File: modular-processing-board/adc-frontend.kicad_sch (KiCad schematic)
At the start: 70 parts, among them J1001 BWU.FL-IPEX1, J601 Conn_Coaxial_Small, J602 BWU.FL-IPEX1, J604 Conn_Coaxial_Small, U1002 THS4521IDGK, U601 LMV321, U602 TL432DBZ, U603 THS4521IDGK

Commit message: matched PSSI bus lenghts
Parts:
- C1012, C1016, C609, C615: LCSC Part Number C1634 -> (none); Manufacturing Part Number CL10C100JB8NNNC -> (none)
- C1015, C611: LCSC Part Number C1664 -> (none); Manufacturing Part Number CL10C331JB8NNNC -> (none)
- C1024, C601, C604, C605, C606, C607, C608, C617: LCSC Part Number C22435929 -> (none); Manufacturing Part Number CGA0201X7R104K160ET -> (none)
- C1025, C602, C618: LCSC Part Number C285010 -> (none); Manufacturing Part Number 0201B103K250NT -> (none)
- C603: LCSC Part Number C16772 -> (none); Manufacturing Part Number CL05B224KO5NNNC -> (none)
- C610, C612, C613, C614: LCSC Part Number C88136 -> (none); Manufacturing Part Number 0603B104J500NT -> (none)
- C616, C619: LCSC Part Number C23733 -> (none); Manufacturing Part Number CL05A475MP5NRNC -> (none)
- J1001, J602: LCSC Part Number C5137195 -> (none); Manufacturing Part Number BWU.FL-IPEX1 -> (none)
- J601, J604: LCSC Part Number C496549 -> (none); Manufacturing Part Number BWSMA-KE-Z001 -> (none)
- R1001, R620: LCSC Part Number C21189 -> (none); Manufacturing Part Number 0603WAF0000T5E -> (none)
- R1006, R608, R609, R610, R612, R627, R628, R629: LCSC Part Number C25804 -> (none); Manufacturing Part Number 0603WAF1002T5E -> (none)
- R1009, R1013, R1021, R1024, R601, R611, R613, R619, R621: LCSC Part Number C21190 -> (none); Manufacturing Part Number 0603WAF1001T5E -> (none)
- R1015, R616: LCSC Part Number C17168 -> (none); Manufacturing Part Number 0402WGF0000TCE -> (none)
- R1016, R1019, R614, R615, R617, R618, R625, R626: LCSC Part Number C23182 -> (none); Manufacturing Part Number 0603WAF470JT5E -> (none)
- R602: LCSC Part Number C4275 -> (none); Manufacturing Part Number 0603WAF750JT5E -> (none)
- R603, R605, R606: LCSC Part Number 0603WAF1001T5E -> (none); Manufacturing Part Number C21190 -> (none)
- R604: LCSC Part Number C22843 -> (none); Manufacturing Part Number 0603WAF1501T5E -> (none)
- R607: LCSC Part Number C23162 -> (none); Manufacturing Part Number 0603WAF4701T5E -> (none)
- U1002, U603: LCSC Part Number C170157 -> (none); Manufacturing Part Number THS4521IDGKR -> (none)
- U601: LCSC Part Number C7972 -> (none); Manufacturing Part Number LMV321IDBVR -> (none)
- U602: LCSC Part Number C5184435 -> (none); Manufacturing Part Number TL432 -> (none)

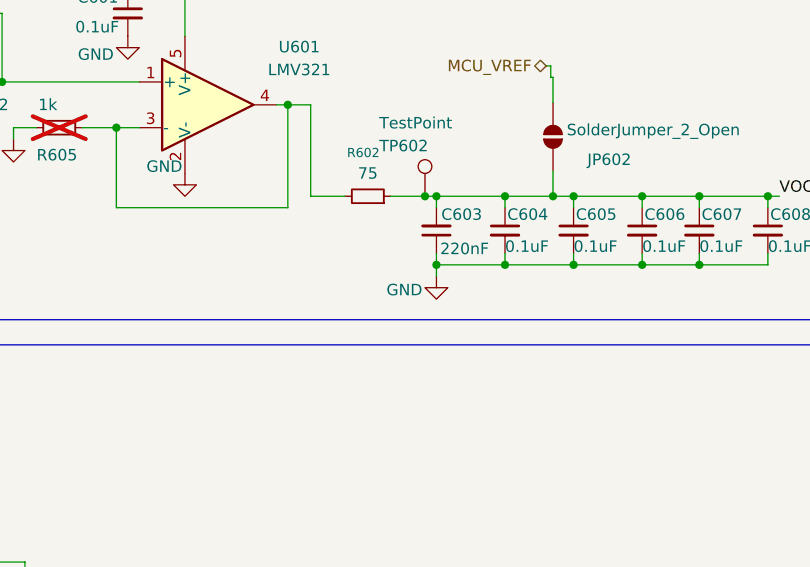
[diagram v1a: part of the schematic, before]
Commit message: finish modular-processing-hw board checks, prepare gerbers for manufacturing and perform checks
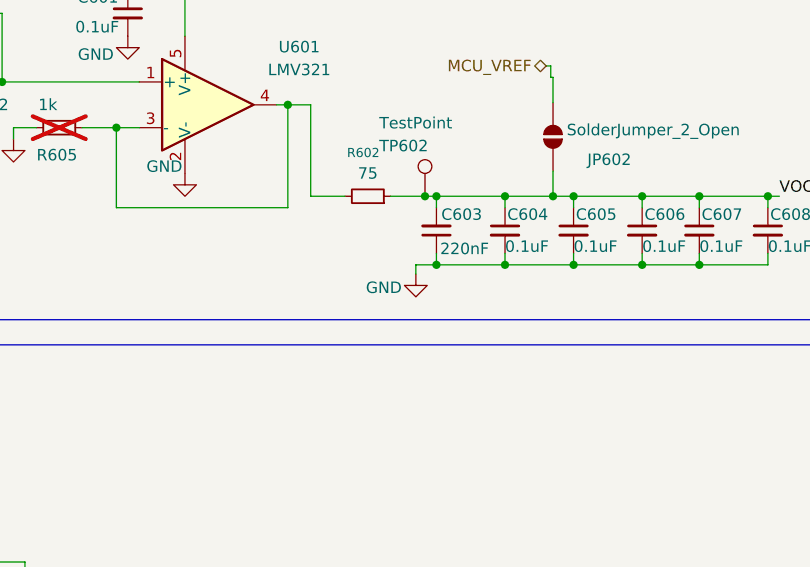
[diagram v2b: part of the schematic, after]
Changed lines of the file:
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@@
 	(wire
 		(pts
-			(xy 181.61 68.58) (xy 181.61 67.31)
+			(xy 179.324 68.326) (xy 179.324 67.31)
 		)
 		(stroke
@@
 	(wire
 		(pts
+			(xy 179.324 67.31) (xy 181.61 67.31)
+		)
+		(stroke
+			(width 0)
+			(type default)
+		)
+	)
+	(wire
+		(pts
 			(xy 175.26 123.19) (xy 175.26 127)
 		)
@@
 	(symbol
 		(lib_id "power:GND")
-		(at 181.61 68.58 0)
+		(at 179.324 68.326 0)
 		(mirror y)
 		(unit 1)
@@
 		(dnp no)
 		(property "Reference" "#PWR0607"
-			(at 181.61 74.93 0)
+			(at 179.324 74.676 0)
 			(effects
 				(font
@@
 		)
 		(property "Value" "GND"
-			(at 178.054 70.104 0)
+			(at 175.768 69.85 0)
 			(effects
 				(font
@@
 		)
 		(property "Footprint" ""
-			(at 181.61 68.58 0)
+			(at 179.324 68.326 0)
 			(effects
 				(font
@@
 		)
 		(property "Datasheet" ""
-			(at 181.61 68.58 0)
+			(at 179.324 68.326 0)
 			(effects
 				(font
@@
 		)
 		(property "Description" "Power symbol creates a global label with name \"GND\" , ground"
-			(at 181.61 68.58 0)
+			(at 179.324 68.326 0)
 			(effects
 				(font

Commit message: minor changes in BOM and DNP-components
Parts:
- C1025, C602, C618: footprint Capacitor_SMD:C_0201_0603Metric -> Capacitor_SMD:C_0402_1005Metric; LPN C285010 -> C15195; MPN 0201B103K250NT -> CL05B103KB5NNNC
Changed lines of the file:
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@@
 			)
 		)
-		(property "Footprint" "Capacitor_SMD:C_0201_0603Metric"
+		(property "Footprint" "Capacitor_SMD:C_0402_1005Metric"
 			(at 113.03 146.05 0)
 			(effects
@@
 			)
 		)
-		(property "LPN" "C285010 "
+		(property "LPN" "C15195"
 			(at 113.03 146.05 0)
 			(effects
@@
 			)
 		)
-		(property "MPN" "0201B103K250NT"
+		(property "MPN" "CL05B103KB5NNNC"
 			(at 113.03 146.05 0)
 			(effects
@@
 			)
 		)
-		(property "Footprint" "Capacitor_SMD:C_0201_0603Metric"
+		(property "Footprint" "Capacitor_SMD:C_0402_1005Metric"
 			(at 121.92 255.27 0)
 			(effects
@@
 			)
 		)
-		(property "LPN" "C285010 "
+		(property "LPN" "C15195"
 			(at 121.92 255.27 0)
 			(effects
@@
 			)
 		)
-		(property "MPN" "0201B103K250NT"
+		(property "MPN" "CL05B103KB5NNNC"
 			(at 121.92 255.27 0)
 			(effects
@@
 			)
 		)
-		(property "Footprint" "Capacitor_SMD:C_0201_0603Metric"
+		(property "Footprint" "Capacitor_SMD:C_0402_1005Metric"
 			(at 127 50.8 0)
 			(effects
@@
 			)
 		)
-		(property "LPN" "C285010 "
+		(property "LPN" "C15195"
 			(at 127 50.8 0)
 			(effects
@@
 			)
 		)
-		(property "MPN" "0201B103K250NT"
+		(property "MPN" "CL05B103KB5NNNC"
 			(at 127 50.8 0)
 			(effects

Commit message: changed footprints (next) try uploading to jlcpcb for manufacturing, change crystal if required for economic assembly
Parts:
- C610, C612, C613, C614: value 100 nF +-5% -> 100nF; footprint Capacitor_SMD:C_0603_1608Metric_Pad1.08x0.95mm_HandSolder -> Capacitor_SMD:C_0603_1608Metric; LPN C88136 -> C14663; MPN 0603B104J500NT -> CC0603KRX7R9BB104
- R1001, R620: footprint Resistor_SMD:R_0603_1608Metric_Pad0.98x0.95mm_HandSolder -> Resistor_SMD:R_0603_1608Metric
- R1015, R616: footprint Resistor_SMD:R_0402_1005Metric_Pad0.72x0.64mm_HandSolder -> Resistor_SMD:R_0603_1608Metric; LPN C17168 -> C21189; MPN 0402WGF0000TCE -> 0603WAF0000T5E
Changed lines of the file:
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@@
 			)
 		)
-		(property "Value" "100 nF +-5%"
+		(property "Value" "100nF"
 			(at 54.102 128.524 90)
 			(effects
@@
 			)
 		)
-		(property "Footprint" "Capacitor_SMD:C_0603_1608Metric_Pad1.08x0.95mm_HandSolder"
+		(property "Footprint" "Capacitor_SMD:C_0603_1608Metric"
 			(at 46.99 125.73 0)
 			(effects
@@
 			)
 		)
-		(property "LPN" "C88136"
+		(property "LPN" "C14663"
 			(at 46.99 125.73 90)
 			(effects
@@
 			)
 		)
-		(property "MPN" "0603B104J500NT"
+		(property "MPN" "CC0603KRX7R9BB104"
 			(at 46.99 125.73 90)
 			(effects
@@
 			)
 		)
-		(property "Footprint" "Resistor_SMD:R_0603_1608Metric_Pad0.98x0.95mm_HandSolder"
+		(property "Footprint" "Resistor_SMD:R_0603_1608Metric"
 			(at 175.26 140.97 0)
 			(effects
@@
 			)
 		)
-		(property "Footprint" "Resistor_SMD:R_0402_1005Metric_Pad0.72x0.64mm_HandSolder"
+		(property "Footprint" "Resistor_SMD:R_0603_1608Metric"
 			(at 95.25 242.57 0)
 			(effects
@@
 			)
 		)
-		(property "LPN" "C17168"
+		(property "LPN" "C21189"
 			(at 95.25 242.57 90)
 			(effects
@@
 			)
 		)
-		(property "MPN" "0402WGF0000TCE"
+		(property "MPN" "0603WAF0000T5E"
 			(at 95.25 242.57 90)
 			(effects
@@
 			)
 		)
-		(property "Footprint" "Resistor_SMD:R_0603_1608Metric_Pad0.98x0.95mm_HandSolder"
+		(property "Footprint" "Resistor_SMD:R_0603_1608Metric"
 			(at 175.26 120.65 0)
 			(effects
@@
 			)
 		)
-		(property "Value" "100 nF +-5%"
+		(property "Value" "100nF"
 			(at 55.372 138.43 90)
 			(effects
@@
 			)
 		)
-		(property "Footprint" "Capacitor_SMD:C_0603_1608Metric_Pad1.08x0.95mm_HandSolder"
+		(property "Footprint" "Capacitor_SMD:C_0603_1608Metric"
 			(at 46.99 135.89 0)
 			(effects
@@
 			)
 		)
-		(property "LPN" "C88136"
+		(property "LPN" "C14663"
 			(at 46.99 135.89 90)
 			(effects
@@
 			)
 		)
-		(property "MPN" "0603B104J500NT"
+		(property "MPN" "CC0603KRX7R9BB104"
 			(at 46.99 135.89 90)
 			(effects
@@
 			)
 		)
-		(property "Value" "100 nF +-5%"
+		(property "Value" "100nF"
 			(at 50.292 237.744 90)
 			(effects
@@
 			)
 		)
-		(property "Footprint" "Capacitor_SMD:C_0603_1608Metric_Pad1.08x0.95mm_HandSolder"
+		(property "Footprint" "Capacitor_SMD:C_0603_1608Metric"
 			(at 43.18 234.95 0)
 			(effects
@@
 			)
 		)
-		(property "LPN" "C88136"
+		(property "LPN" "C14663"
 			(at 43.18 234.95 90)
 			(effects
@@
 			)
 		)
-		(property "MPN" "0603B104J500NT"
+		(property "MPN" "CC0603KRX7R9BB104"
 			(at 43.18 234.95 90)
 			(effects
@@
 			)
 		)
-		(property "Value" "100 nF +-5%"
+		(property "Value" "100nF"
 			(at 51.562 247.65 90)
 			(effects
@@
 			)
 		)
-		(property "Footprint" "Capacitor_SMD:C_0603_1608Metric_Pad1.08x0.95mm_HandSolder"
+		(property "Footprint" "Capacitor_SMD:C_0603_1608Metric"
 			(at 43.18 245.11 0)
 			(effects
@@
 			)
 		)
-		(property "LPN" "C88136"
+		(property "LPN" "C14663"
 			(at 43.18 245.11 90)
 			(effects
@@
 			)
 		)
-		(property "MPN" "0603B104J500NT"
+		(property "MPN" "CC0603KRX7R9BB104"
 			(at 43.18 245.11 90)
 			(effects
@@
 			)
 		)
-		(property "Footprint" "Resistor_SMD:R_0402_1005Metric_Pad0.72x0.64mm_HandSolder"
+		(property "Footprint" "Resistor_SMD:R_0603_1608Metric"
 			(at 90.17 133.35 0)
 			(effects
@@
 			)
 		)
-		(property "LPN" "C17168"
+		(property "LPN" "C21189"
 			(at 90.17 133.35 90)
 			(effects
@@
 			)
 		)
-		(property "MPN" "0402WGF0000TCE"
+		(property "MPN" "0603WAF0000T5E"
 			(at 90.17 133.35 90)
 			(effects

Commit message: changed testpoints
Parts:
- TP601: footprint TestPoint:TestPoint_Pad_1.0x1.0mm -> Connector_PinSocket_1.27mm:PinSocket_1x01_P1.27mm_Vertical
- TP602: footprint iw-misc:TestPoint_Pad_D0.5mm -> Connector_PinSocket_1.27mm:PinSocket_1x01_P1.27mm_Vertical
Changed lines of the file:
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@@
 			)
 		)
-		(property "Footprint" "TestPoint:TestPoint_Pad_1.0x1.0mm"
+		(property "Footprint" "Connector_PinSocket_1.27mm:PinSocket_1x01_P1.27mm_Vertical"
 			(at 120.65 39.37 0)
 			(effects
@@
 			)
 		)
-		(property "Footprint" "iw-misc:TestPoint_Pad_D0.5mm"
+		(property "Footprint" "Connector_PinSocket_1.27mm:PinSocket_1x01_P1.27mm_Vertical"
 			(at 185.42 59.69 0)
 			(effects
